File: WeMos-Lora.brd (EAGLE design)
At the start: 33.3 x 25.7 mm, 21 parts, among them P1 PADNORMAL, P2 PADNORMAL, P3 PADNORMAL, P4 PADNORMAL

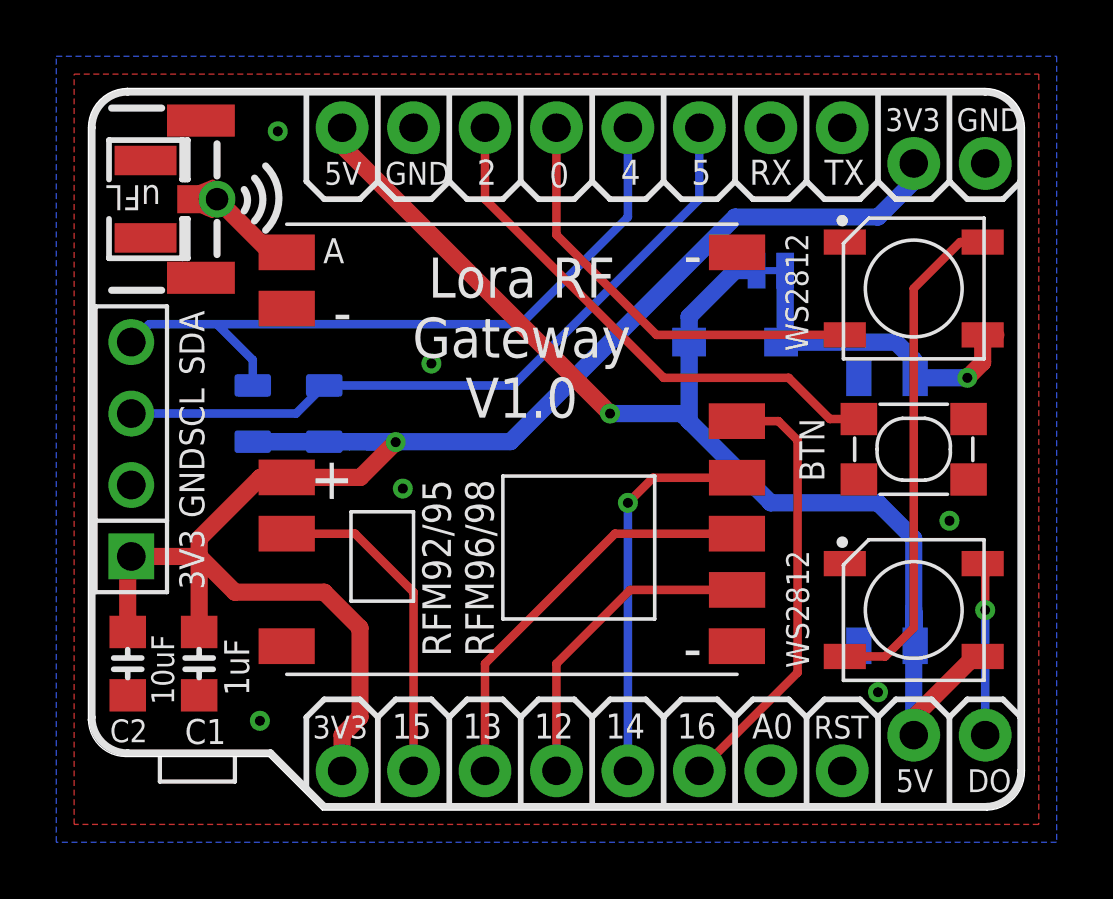
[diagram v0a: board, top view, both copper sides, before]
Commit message: Version V1.1
- OLED Display connector has now lock pad
- Antenna signal with via all around
- ground plane set to 12min blocking to avoid short circuit with
connectors in rarely cases
- Added footprint for Microchip 24AA02E64 64 bits serial number
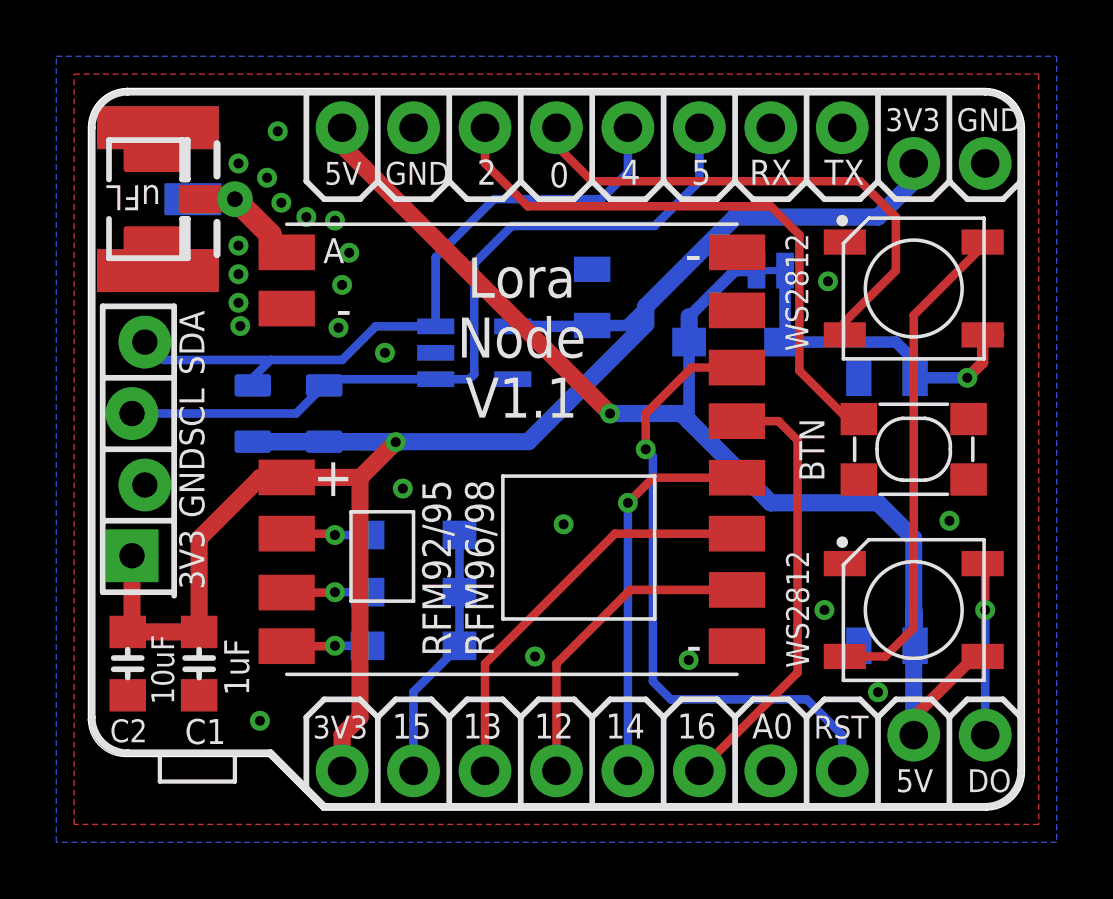
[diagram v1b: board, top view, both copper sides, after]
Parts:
- removed J$1: ANTENNASMALL, _c2h:SMA_UFL_PAD_SMALL
- added C5: 100nF, _c2h:0805-CAP
- added D2, D3, D4: 1N4148, Seeed-Discrete:SOD123-2.7X1.6
- added J$2: ANTENNATINY, _c2h:SMA_UFL_PAD_TINY
- added U1: 24AA02E64T, Microchip-24AA02E64T:SOT95P270X145-5N
- I2C_OLED: value CON_HEADER_1X04'SMALL'' -> CON_HEADER_1X04'LOCK'; device _c2h:M1X4 -> _c2h:1X04_LOCK
- moved I2C_OLED 5.27 mm to (5.97, 7.62)
- moved U$4 2.62 mm to (22.7, 5.97)
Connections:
- new net DIO0: D2.1, U$5.DIO0
- new net DIO1: D3.1, U$5.DIO1
- new net DIO2: D4.1, U$5.DIO2
- net 3V3: now also C5.1, U1.4
- net ANT: now also J$2.ANT1, J$2.ANT2, J$2.ANT3; no longer J$1.ANT1, J$1.ANT2
- net GND: now also C5.2, J$2.GND1, J$2.GND2, J$2.GND3, J$2.GND4, U1.2; no longer J$1.GND1, J$1.GND2, J$1.GND3, J$1.GND4
- net GPIO15: now also D2.2, D3.2, D4.2; no longer U$5.DIO0
- net RST: now also U$5.RST
- net SCL: now also U1.1
- net SDA: now also U1.3
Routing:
- net RST: track 0.00 -> 22.3 mm, vias 0 -> 1
- net 3V3: track 62.0 -> 66.1 mm
- net GPIO0: track 15.5 -> 18.7 mm
- net DIO1: track 0.00 -> 2.90 mm, vias 0 -> 1
- net DIO0: track 0.00 -> 2.89 mm, vias 0 -> 1
- net DIO2: track 0.00 -> 2.88 mm, vias 0 -> 1
- net GPIO15: track 11.7 -> 9.06 mm
- net GPIO2: track 19.1 -> 21.2 mm
- net SCL: track 25.9 -> 27.8 mm
- net ANT: track 4.28 -> 5.73 mm
- net SDA: track 25.4 -> 24.4 mm
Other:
- board text added: "Lora Node"
- board text added: "Lora Node V1.1"
- board text removed: "Lora RF Gateway V1.0"
- board text removed: "V1.0"
- board text removed: "WeMos Lora GW"

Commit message: Bump to V1.2
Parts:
- added JP3: DS, _c2h:PAD-JUMPER-3-2OF3_NC_BY_TRACE_YES_SILK_FULL_BOX
- added R3: 100K, _c2h:0805-RES
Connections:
- new net SEL: JP3.3, R3.2, U$5.NSS
- net GND: now also R3.1
- net GPIO16: now also JP3.2; no longer U$5.NSS
- net RST: now also JP3.1
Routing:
- net SEL: track 0.00 -> 19.5 mm, vias 0 -> 1
- net RST: track 22.3 -> 27.0 mm, vias 1 -> 2
- net GPIO16: track 15.6 -> 13.7 mm, vias 0 -> 1
- net 5V: track 46.9 -> 48.1 mm
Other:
- board text added: "24AA02"
- board text added: "GPIO"
- board text added: "Lora Node V1.2"
- board text added: "SEL"
- board text added: "V1.2"
- board text removed: "Lora Node V1.1"

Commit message: Bump to v1.3
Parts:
- added U$2: PAD-JUMPER-SWAPSWAP, _c2h:PAD-JUMPER-SWAP
- moved U$4 0.28 mm to (22.5, 5.71)
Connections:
- new net 3V3_GD: I2C_OLED.1, U$2.3
- new net GD_3V3: I2C_OLED.2, U$2.2
- net 3V3: now also U$2.4, U$2.44; no longer I2C_OLED.1
- net GND: now also U$2.1, U$2.11; no longer I2C_OLED.2
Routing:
- net 3V3_GD: track 0.00 -> 6.32 mm
- net GD_3V3: track 0.00 -> 3.95 mm
- net 3V3: track 66.1 -> 68.3 mm, vias 1 -> 2
- net GND: track 0.00 -> 1.78 mm, vias 26 -> 28
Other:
- board text added: "Lora Node V1.3"
- board text added: "V1.3"
- board text removed: "I2C PUP"
- board text removed: "Lora Node V1.2"
- board text removed: "V1.2"
